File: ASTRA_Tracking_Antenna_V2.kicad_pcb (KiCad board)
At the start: 2 copper layers, 84.3 x 130.6 mm, 21 parts, among them J2 24V, J3 24V, J4 24V, J5 5V, J6 Conn_01x04_Socket, M1 Stepper_Motor_bipolar, U4 D24V22F3, U5 D24V22F5

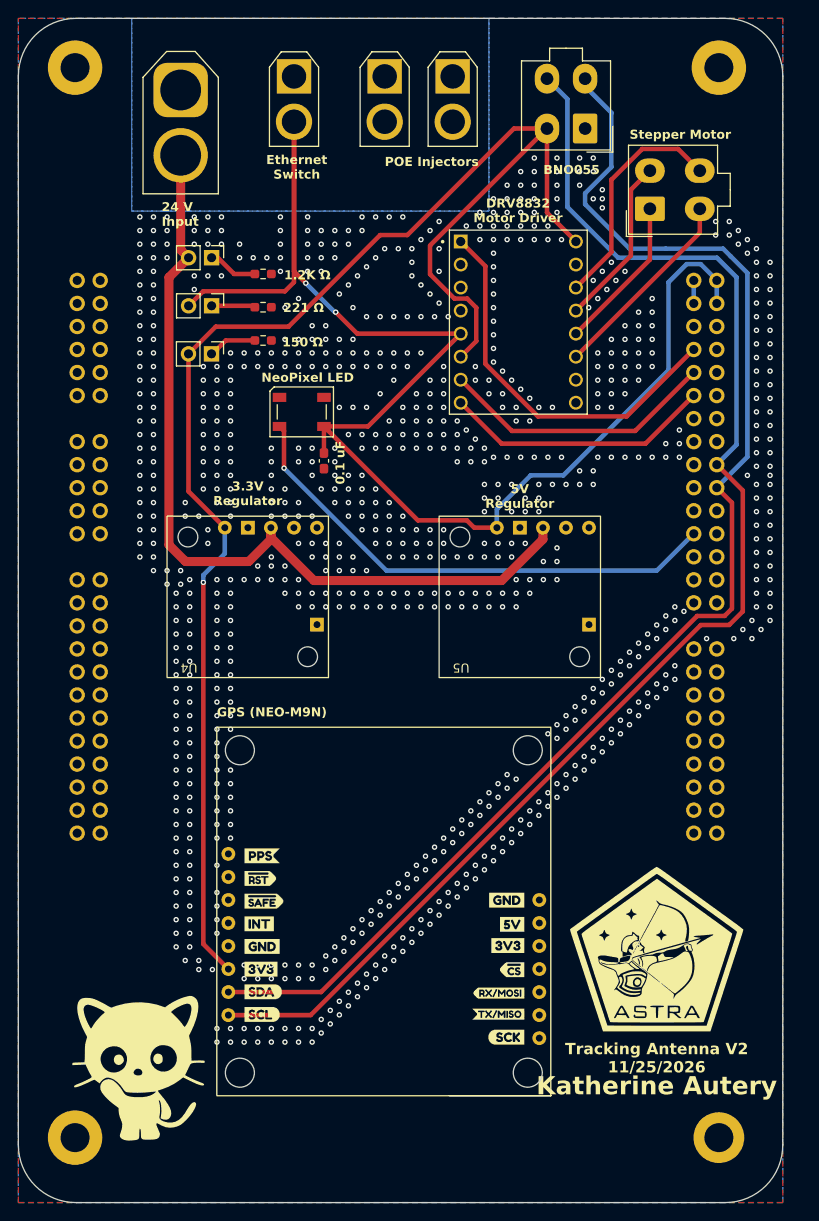
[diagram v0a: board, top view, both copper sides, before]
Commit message: PCB Created With SMD Driver
Tracking Antenna PCB revised to incorporate an SMD motor driver, and extraneous files also cleaned up.
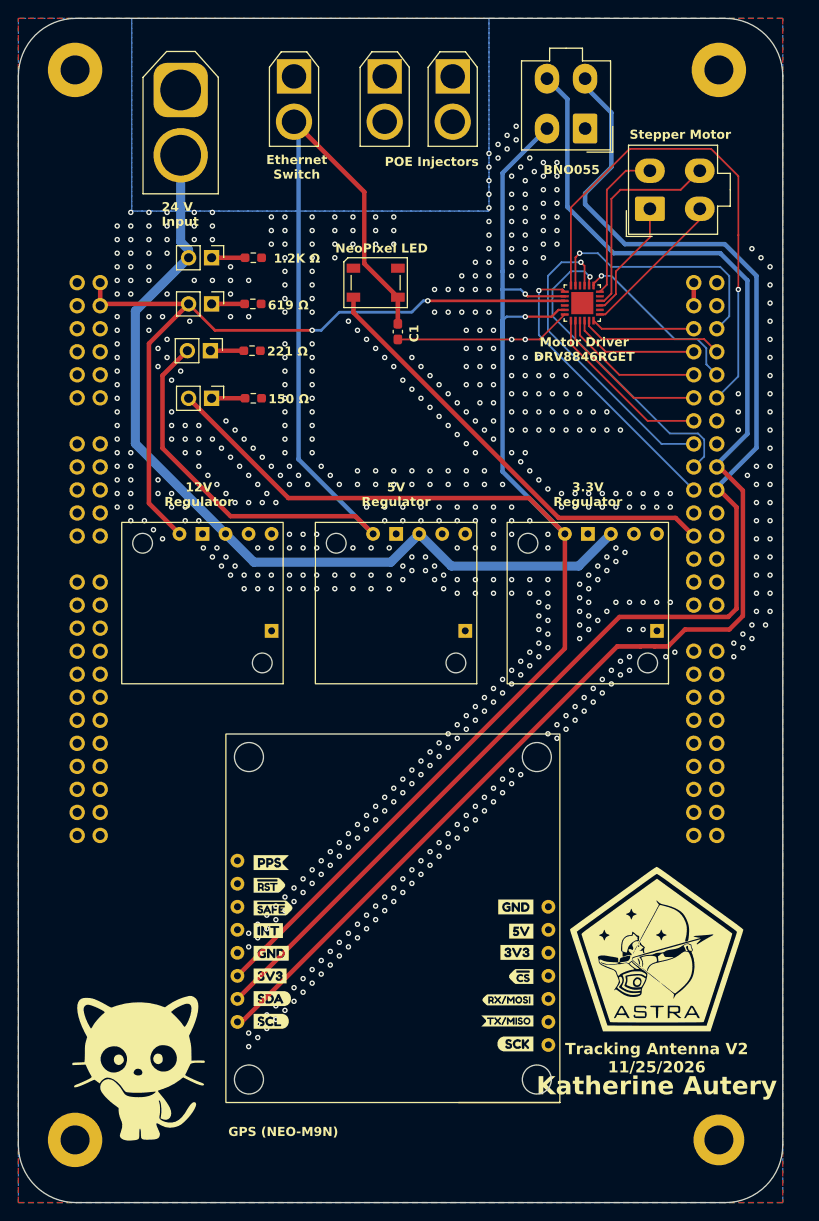
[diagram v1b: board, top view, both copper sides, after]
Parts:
- removed 1: DRV8834, Tracking Ant:Polulu_DRV8834
- added D5: LED, Tracking Ant:LED 3mm, F.Cu at (175.9, 55.1)
- added R2: 619Ω, Resistor_SMD:R_0603_1608Metric_Pad0.98x0.95mm_HandSolder, F.Cu at (180.5, 55.1)
- added U2: D24V22F12, Tracking Ant:D24V22Fx, F.Cu at (183.8, 97.0)
- added U3: DRV8846RGET, Tracking Ant:DRV8846, F.Cu at (216.8, 55.0)
- C1: renamed from 0.1 uF
- M1: value Stepper_Motor_bipolar -> Stepper Motor
- moved U4 37.5 mm to (226.3, 97.0)
- moved D2 16.4 mm to (194.0, 52.8)
- moved C1 16.4 mm to (196.4, 58.1)
- moved U5 13.7 mm to (205.2, 97.0)
- moved R4 6.47 mm to (180.5, 65.5)
- moved D3 4.95 mm to (175.8, 60.2)
- moved R3 4.95 mm to (180.4, 60.2)
- moved D4 4.90 mm to (175.9, 65.5)
- moved R1 2.09 mm to (180.5, 50.0)
- moved U1 1.25 mm to (214.3, 102.5)
- moved A1 0.25 mm to (231.6, 52.8)
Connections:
- A1 pad 1: +5V -> unconnected-(A1A-+5V-Pad1)
- A1 pad 10: /Motor_Step -> /CurrentScalar1_Driver
- A1 pad 11: unconnected-(A1A-D6-Pad11) -> /Step_Driver
- A1 pad 12: /Motor_Dir -> /CurrentScalar0_Driver
- A1 pad 14: unconnected-(A1A-D12-Pad14) -> /ADEC_Driver
- A1 pad 16: unconnected-(A1A-D11-Pad16) -> /Micro1_Driver
- A1 pad 18: unconnected-(A1A-D10-Pad18) -> /Micro0_Driver
- A1 pad 20: unconnected-(A1A-D9-Pad20) -> /Dir_Driver
- A1 pad 3: +5V -> unconnected-(A1A-+5V-Pad3)
- A1 pad 5: unconnected-(A1A-A2-Pad5) -> /Enable_Driver
- A1 pad 51: unconnected-(A1B-+DC_IN-Pad51) -> +12V
- A1 pad 52: unconnected-(A1B-GND-Pad52) -> GND
- A1 pad 53: unconnected-(A1B-+DC_IN-Pad53) -> +12V
- A1 pad 54: unconnected-(A1B-GND-Pad54) -> GND
- A1 pad 6: unconnected-(A1A-A5-Pad6) -> /Decay1_Driver
- A1 pad 7: unconnected-(A1A-A1-Pad7) -> /Sleep_Driver
- A1 pad 8: /EN_Driver -> /Decay0_Driver
- A1 pad 9: unconnected-(A1A-A0-Pad9) -> /nFault_Driver
- M1 pad 1: /A1_Motor -> /A2_Motor
- M1 pad 3: /A2_Motor -> /A1_Motor
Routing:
- net +12V: track 0.00 -> 85.0 mm, vias 0 -> 2
- net /Step_Driver: track 0.00 -> 56.4 mm, vias 0 -> 1
- net +5V: track 161.4 -> 115.1 mm, vias 2 -> 0
- net /EN_Driver: track 43.1 -> 0.00 mm
- net /Micro0_Driver: track 0.00 -> 35.0 mm, vias 0 -> 1
- net /Micro1_Driver: track 0.00 -> 34.3 mm, vias 0 -> 1
- net /Dir_Driver: track 0.00 -> 32.1 mm, vias 0 -> 1
- net /Motor_Step: track 30.7 -> 0.00 mm
- net /Motor_Dir: track 29.8 -> 0.00 mm
- net /Enable_Driver: track 0.00 -> 27.7 mm, vias 0 -> 1
- net /nFault_Driver: track 0.00 -> 19.8 mm, vias 0 -> 1
- net /ADEC_Driver: track 0.00 -> 19.7 mm
- net GND: track 2.54 -> 22.1 mm, vias 868 -> 652
- net /CurrentScalar0_Driver: track 0.00 -> 17.8 mm
- net /CurrentScalar1_Driver: track 0.00 -> 16.0 mm
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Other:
- board text added: "12V Regulator"
- board text added: "619 Ω"
- board text added: "Motor Driver DRV8846RGET"
- board text removed: "DRV8832 Motor Driver"

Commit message: PCB Revisions from Feedback and Drone
Revisions made to PCB based on feedback, 3.3V Reg swapped, corrections made to motor driver, connector added for drone subteam.
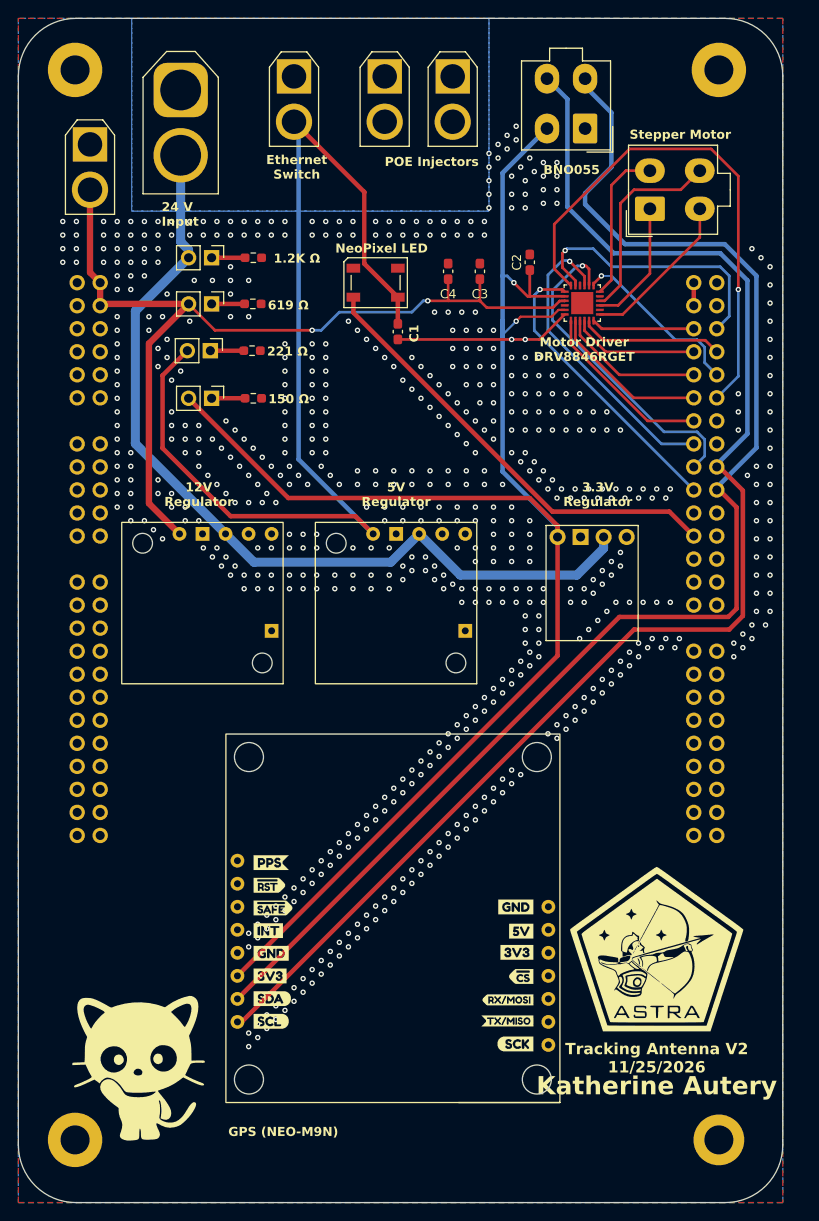
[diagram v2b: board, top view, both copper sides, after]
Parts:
- added C2: 2.2 μF, Capacitor_SMD:C_0603_1608Metric_Pad1.08x0.95mm_HandSolder, F.Cu at (211.0, 50.5)
- added C3: 10 μF, Capacitor_SMD:C_0603_1608Metric_Pad1.08x0.95mm_HandSolder, F.Cu at (205.5, 51.5)
- added C4: 0.1 μF, Capacitor_SMD:C_0603_1608Metric_Pad1.08x0.95mm_HandSolder, F.Cu at (202.0, 51.5)
- added J1: Conn_01x02_Socket, Tracking Ant:XT30F_MODIFIED, F.Cu at (162.5, 37.5)
- U4: value D24V22F3 -> D36V6F3; footprint Tracking Ant:D24V22Fx -> Tracking Ant:D36V6F3 3.3V
- moved U4 16.8 mm to (221.7, 80.8)
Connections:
- U4 pad 2: unconnected-(U4-EN-Pad2) -> +24V
- U4 pad 3: +24V -> GND
- U4 pad 4: GND -> +3.3V
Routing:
- net +12V: track 85.0 -> 101.1 mm
- net +3.3V: track 178.0 -> 183.1 mm
- net /Enable_Driver: track 27.7 -> 30.5 mm
- net /Step_Driver: track 56.4 -> 57.9 mm
- net /Micro0_Driver: track 35.0 -> 36.2 mm
- net /A1_Motor: track 16.6 -> 17.7 mm
- net /A2_Motor: track 13.3 -> 14.1 mm
- net /B2_Motor: track 23.1 -> 22.3 mm
- net +24V: track 97.7 -> 98.3 mm
- net GND: vias 652 -> 659

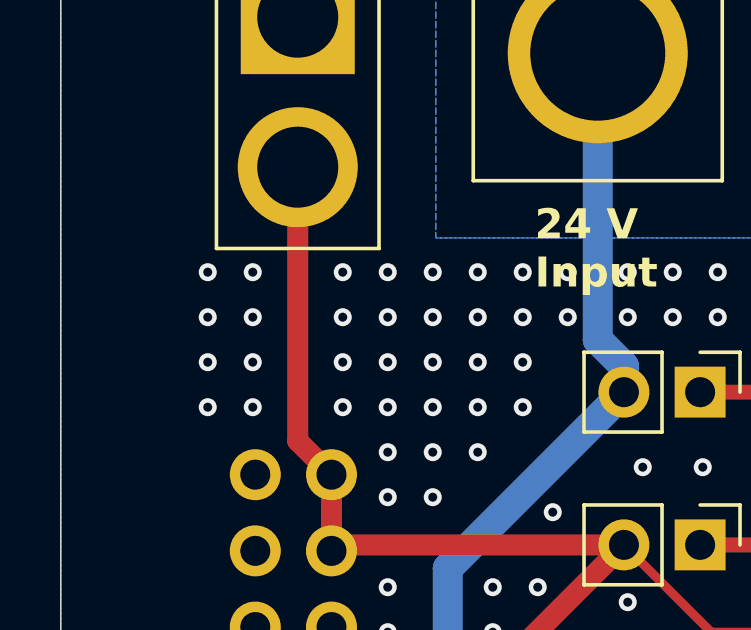
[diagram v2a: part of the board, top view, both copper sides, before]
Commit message: Silkscreen Addition
Label added on silkscreen for an output connection
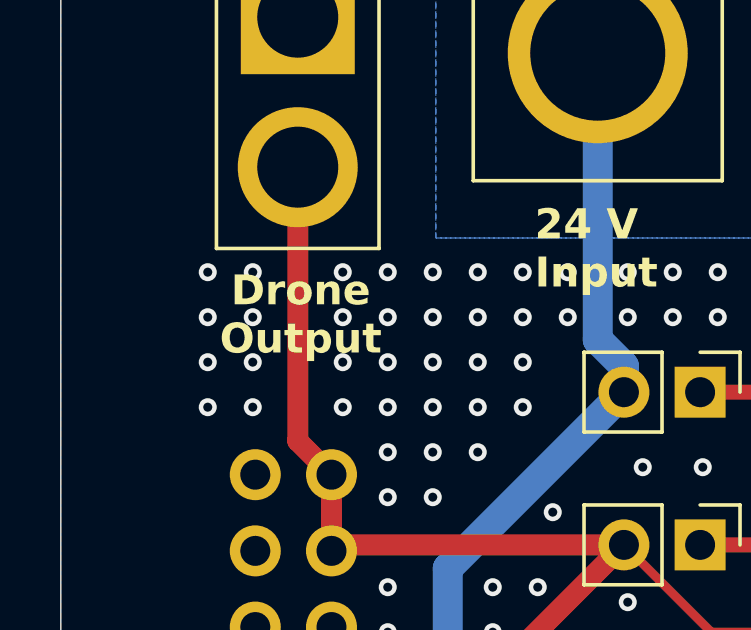
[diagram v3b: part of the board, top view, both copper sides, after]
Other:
- board text added: "Drone Output"
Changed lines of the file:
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@@
 		(layer "Edge.Cuts")
+	)
+	(gr_text "Drone\nOutput"
+		(at 162.6 48.8 0)
+		(layer "F.SilkS")
+		(effects
+			(font
+				(size 0.99822 0.99822)
+				(thickness 0.199644)
+				(bold yes)
+			)
+			(justify bottom)
+		)
 	)
 	(gr_text "12V\nRegulator"

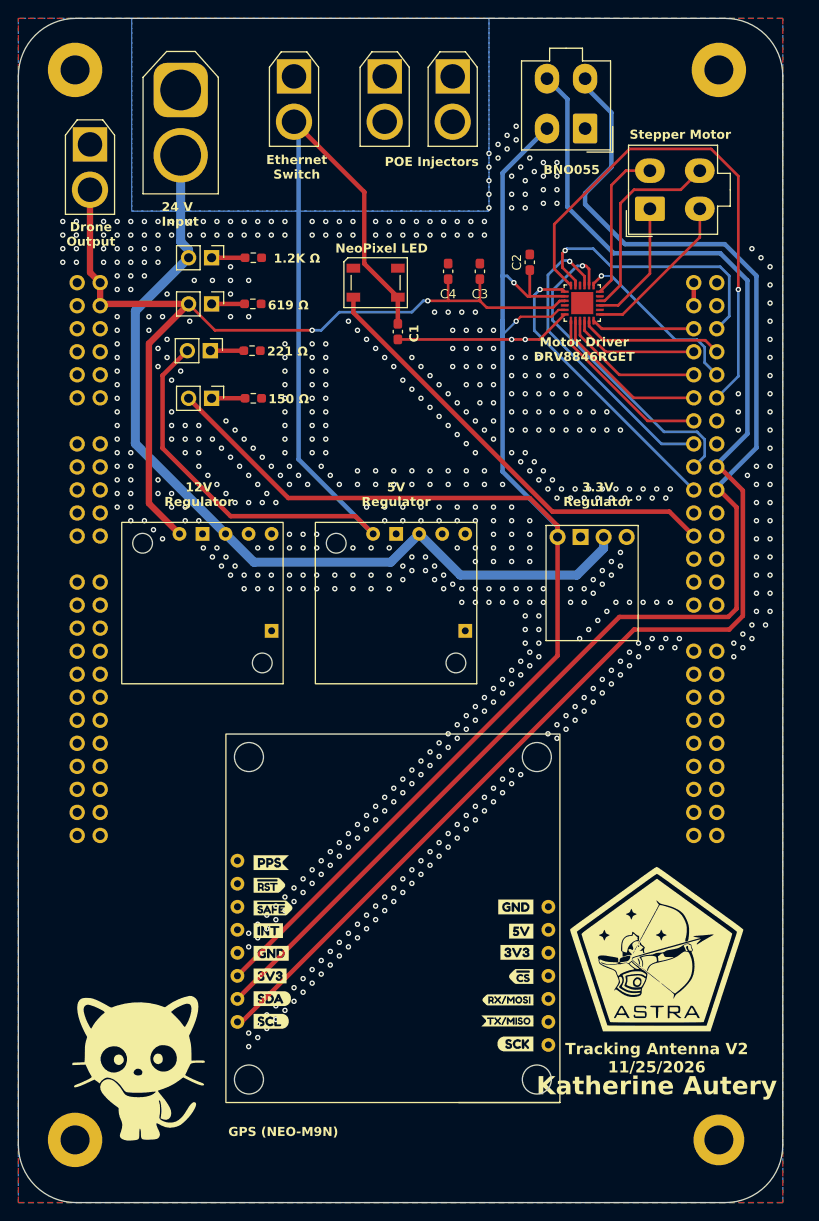
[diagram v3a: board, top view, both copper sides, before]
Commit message: Final Tracking Antenna V2
Tracking Antenna final revisions, PCB ordered, drill and gerber files included.
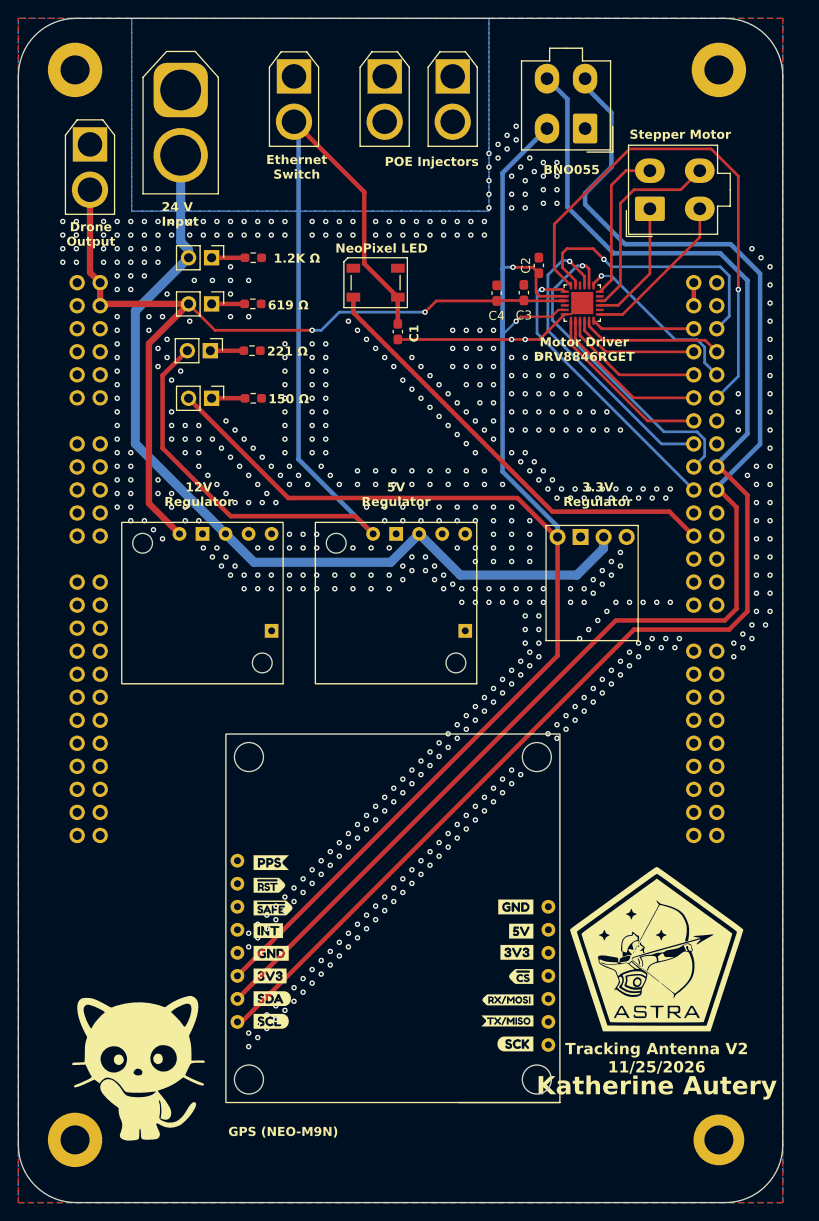
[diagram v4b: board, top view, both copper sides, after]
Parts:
- moved C4 5.86 mm to (207.3, 53.9)
- moved C3 5.39 mm to (210.3, 53.9)
- moved C2 1.06 mm to (212.0, 50.9)
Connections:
- U3 pad 25: (no net) -> GND
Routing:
- net +12V: track 101.1 -> 96.3 mm
- net GND: track 22.1 -> 24.5 mm, vias 659 -> 655
- net +3.3V: track 183.1 -> 181.4 mm
- net Sensor_SDA: track 150.7 -> 151.4 mm
